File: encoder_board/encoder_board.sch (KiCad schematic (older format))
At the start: 4 parts, among them J1 Conn_01x06, U1 AS5048A

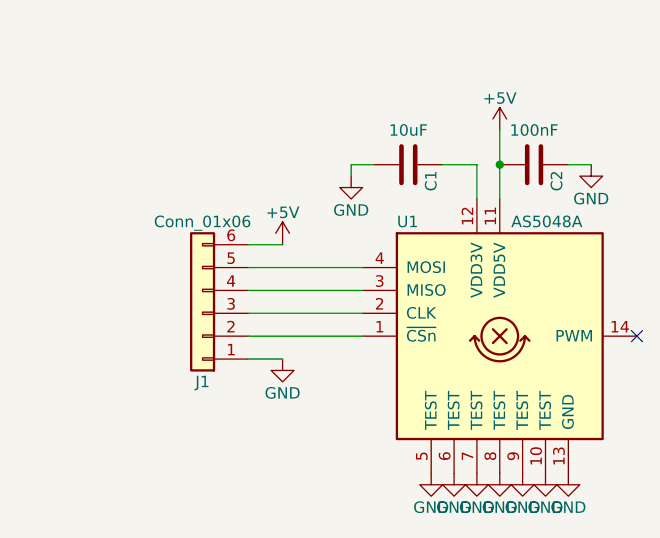
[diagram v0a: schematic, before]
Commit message: add footprint for small ir sensors
 - use 0402 in encoder board
 - still need to switch sensor board
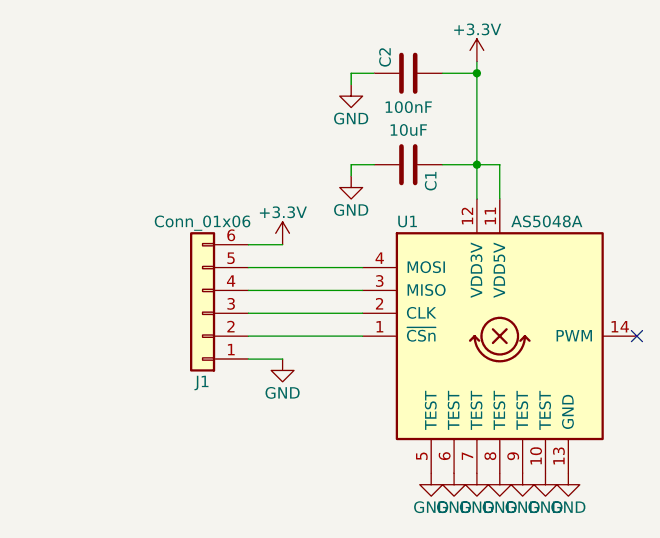
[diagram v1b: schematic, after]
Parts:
- C1, C2: footprint Capacitors_SMD:C_0603 -> Capacitors_SMD:C_0402
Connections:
- net +5V is gone; now on net +3V3: C2.2, J1.6 (Pin_6), U1.11 (VDD5V)
- net +3V3: now reaches C1.1, U1.12 (VDD3V)
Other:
- moved on the sheet: C2
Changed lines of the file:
@@
 LIBS:valves
 LIBS:motor_drivers
-LIBS:LED
 LIBS:sensors
+LIBS:encoder_board-cache
 EELAYER 25 0
 EELAYER END
@@
 F 0 "C1" H 5425 3200 50  0000 L CNN
 F 1 "10uF" V 5250 3100 50  0000 C CNN
-F 2 "Capacitors_SMD:C_0603" H 5438 2950 50  0001 C CNN
+F 2 "Capacitors_SMD:C_0402" H 5438 2950 50  0001 C CNN
 F 3 "" H 5400 3100 50  0001 C CNN
 	1    5400 3100
@@
 F 3 "" H 5150 3150 50  0001 C CNN
 	1    5150 3150
-	1    0    0    -1
-$EndComp
-$Comp
-L +5V #PWR09
-U 1 1 5AAA0D34
-P 5800 2950
-F 0 "#PWR09" H 5800 2800 50  0001 C CNN
-F 1 "+5V" H 5800 3090 50  0000 C CNN
-F 2 "" H 5800 2950 50  0001 C CNN
-F 3 "" H 5800 2950 50  0001 C CNN
-	1    5800 2950
 	1    0    0    -1
 $EndComp
@@
 $EndComp
 $Comp
-L +5V #PWR010
-U 1 1 5AAA0F91
-P 4850 3450
-F 0 "#PWR010" H 4850 3300 50  0001 C CNN
-F 1 "+5V" H 4850 3590 50  0000 C CNN
-F 2 "" H 4850 3450 50  0001 C CNN
-F 3 "" H 4850 3450 50  0001 C CNN
-	1    4850 3450
-	1    0    0    -1
-$EndComp
-$Comp
-L GND #PWR011
+L GND #PWR09
 U 1 1 5AAA0FBB
 P 4850 3950
-F 0 "#PWR011" H 4850 3700 50  0001 C CNN
+F 0 "#PWR09" H 4850 3700 50  0001 C CNN
 F 1 "GND" H 4850 3800 50  0000 C CNN
 F 2 "" H 4850 3950 50  0001 C CNN
@@
 L C C2
 U 1 1 5AAA1099
-P 5950 3100
-F 0 "C2" H 5975 3200 50  0000 L CNN
-F 1 "100nF" V 5800 3100 50  0000 C CNN
-F 2 "Capacitors_SMD:C_0603" H 5988 2950 50  0001 C CNN
-F 3 "" H 5950 3100 50  0001 C CNN
-	1    5950 3100
-	0    1    1    0
+P 5400 2700
+F 0 "C2" H 5425 2800 50  0000 L CNN
+F 1 "100nF" V 5250 2700 50  0000 C CNN
+F 2 "Capacitors_SMD:C_0402" H 5438 2550 50  0001 C CNN
+F 3 "" H 5400 2700 50  0001 C CNN
+	1    5400 2700
+	0    -1   -1   0
 $EndComp
 NoConn ~ 6400 3850
 $Comp
-L GND #PWR012
+L GND #PWR010
 U 1 1 5AAA1198
-P 6200 3100
-F 0 "#PWR012" H 6200 2850 50  0001 C CNN
-F 1 "GND" H 6200 2950 50  0000 C CNN
-F 2 "" H 6200 3100 50  0001 C CNN
-F 3 "" H 6200 3100 50  0001 C CNN
-	1    6200 3100
-	1    0    0    -1
-$EndComp
-Wire Wire Line
-	5550 3100 5700 3100
-Wire Wire Line
-	5700 3100 5700 3250
+P 5150 2750
+F 0 "#PWR010" H 5150 2500 50  0001 C CNN
+F 1 "GND" H 5150 2600 50  0000 C CNN
+F 2 "" H 5150 2750 50  0001 C CNN
+F 3 "" H 5150 2750 50  0001 C CNN
+	1    5150 2750
+	1    0    0    -1
+$EndComp
+$Comp
+L +3.3V #PWR011
+U 1 1 5AAC3FB7
+P 5700 2650
+F 0 "#PWR011" H 5700 2500 50  0001 C CNN
+F 1 "+3.3V" H 5700 2790 50  0000 C CNN
+F 2 "" H 5700 2650 50  0001 C CNN
+F 3 "" H 5700 2650 50  0001 C CNN
+	1    5700 2650
+	1    0    0    -1
+$EndComp
+$Comp
+L +3.3V #PWR012
+U 1 1 5AAC405B
+P 4850 3450
+F 0 "#PWR012" H 4850 3300 50  0001 C CNN
+F 1 "+3.3V" H 4850 3590 50  0000 C CNN
+F 2 "" H 4850 3450 50  0001 C CNN
+F 3 "" H 4850 3450 50  0001 C CNN
+	1    4850 3450
+	1    0    0    -1
+$EndComp
 Wire Wire Line
 	5150 3150 5150 3100
@@
 	5200 3850 4700 3850
 Wire Wire Line
-	5800 2950 5800 3250
-Connection ~ 5800 3100
-Wire Wire Line
-	6100 3100 6200 3100
+	5550 2700 5700 2700
+Wire Wire Line
+	5250 2700 5150 2700
+Wire Wire Line
+	5150 2700 5150 2750
+Wire Wire Line
+	5700 2650 5700 3250
+Connection ~ 5700 2700
+Wire Wire Line
+	5550 3100 5800 3100
+Connection ~ 5700 3100
+Wire Wire Line
+	5800 3100 5800 3250
 $EndSCHEMATC

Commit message: use named nets
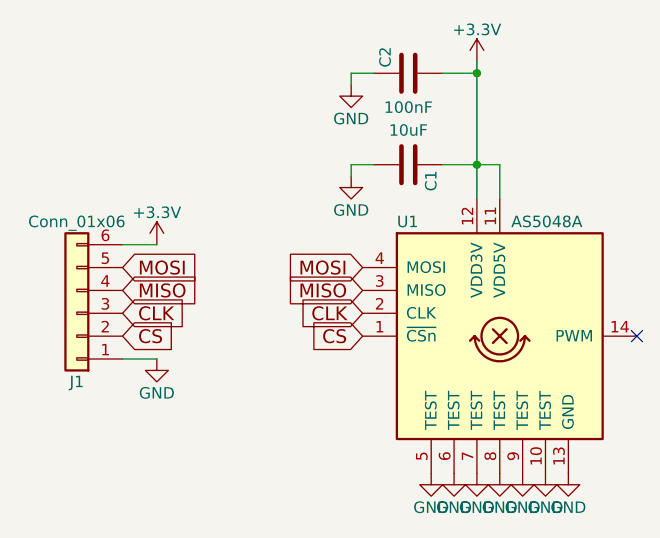
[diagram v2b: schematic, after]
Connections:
- net CS: now reaches J1.2 (Pin_2), U1.1 (~CSn)
- net CLK: now reaches J1.3 (Pin_3), U1.2 (CLK)
- net MISO: now reaches J1.4 (Pin_4), U1.3 (MISO)
- net MOSI: now reaches J1.5 (Pin_5), U1.4 (MOSI)
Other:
- moved on the sheet: J1
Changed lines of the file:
@@
 LIBS:valves
 LIBS:motor_drivers
+LIBS:LED
 LIBS:sensors
 LIBS:encoder_board-cache
@@
 L Conn_01x06 J1
 U 1 1 5AAA0E35
-P 4500 3750
-F 0 "J1" H 4500 4050 50  0000 C CNN
-F 1 "Conn_01x06" H 4500 3350 50  0000 C CNN
-F 2 "Pin_Headers:Pin_Header_Straight_1x06_Pitch1.27mm" H 4500 3750 50  0001 C CNN
-F 3 "" H 4500 3750 50  0001 C CNN
-	1    4500 3750
+P 3950 3750
+F 0 "J1" H 3950 4050 50  0000 C CNN
+F 1 "Conn_01x06" H 3950 3350 50  0000 C CNN
+F 2 "Pin_Headers:Pin_Header_Straight_1x06_Pitch1.27mm" H 3950 3750 50  0001 C CNN
+F 3 "" H 3950 3750 50  0001 C CNN
+	1    3950 3750
 	-1   0    0    1
 $EndComp
@@
 L GND #PWR09
 U 1 1 5AAA0FBB
-P 4850 3950
-F 0 "#PWR09" H 4850 3700 50  0001 C CNN
-F 1 "GND" H 4850 3800 50  0000 C CNN
-F 2 "" H 4850 3950 50  0001 C CNN
-F 3 "" H 4850 3950 50  0001 C CNN
-	1    4850 3950
+P 4300 3950
+F 0 "#PWR09" H 4300 3700 50  0001 C CNN
+F 1 "GND" H 4300 3800 50  0000 C CNN
+F 2 "" H 4300 3950 50  0001 C CNN
+F 3 "" H 4300 3950 50  0001 C CNN
+	1    4300 3950
 	1    0    0    -1
 $EndComp
@@
 L +3.3V #PWR012
 U 1 1 5AAC405B
-P 4850 3450
-F 0 "#PWR012" H 4850 3300 50  0001 C CNN
-F 1 "+3.3V" H 4850 3590 50  0000 C CNN
-F 2 "" H 4850 3450 50  0001 C CNN
-F 3 "" H 4850 3450 50  0001 C CNN
-	1    4850 3450
+P 4300 3450
+F 0 "#PWR012" H 4300 3300 50  0001 C CNN
+F 1 "+3.3V" H 4300 3590 50  0000 C CNN
+F 2 "" H 4300 3450 50  0001 C CNN
+F 3 "" H 4300 3450 50  0001 C CNN
+	1    4300 3450
 	1    0    0    -1
 $EndComp
@@
 	5150 3100 5250 3100
 Wire Wire Line
-	4850 3450 4700 3450
-Wire Wire Line
-	4850 3950 4700 3950
-Wire Wire Line
-	5200 3550 4700 3550
-Wire Wire Line
-	5200 3650 4700 3650
-Wire Wire Line
-	4700 3750 5200 3750
-Wire Wire Line
-	5200 3850 4700 3850
+	4300 3450 4150 3450
+Wire Wire Line
+	4300 3950 4150 3950
 Wire Wire Line
 	5550 2700 5700 2700
@@
 Wire Wire Line
 	5800 3100 5800 3250
+Text GLabel 5200 3550 0    60   Input ~ 0
+MOSI
+Text GLabel 5200 3650 0    60   Input ~ 0
+MISO
+Text GLabel 5200 3750 0    60   Input ~ 0
+CLK
+Text GLabel 5200 3850 0    60   Input ~ 0
+CS
+Text GLabel 4150 3850 2    60   Input ~ 0
+CS
+Text GLabel 4150 3750 2    60   Input ~ 0
+CLK
+Text GLabel 4150 3650 2    60   Input ~ 0
+MISO
+Text GLabel 4150 3550 2    60   Input ~ 0
+MOSI
 $EndSCHEMATC

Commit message: reviewer final encoder board.
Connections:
- net +3V3: now also J1.2 (Pin_2); no longer J1.6 (Pin_6)
- net CLK: now also J1.4 (Pin_4); no longer J1.3 (Pin_3)
- net CS: now also J1.3 (Pin_3); no longer J1.2 (Pin_2)
- net GND: no longer U1.10 (TEST), U1.6 (TEST), U1.7 (TEST), U1.8 (TEST), U1.9 (TEST)
- net MISO: now also J1.5 (Pin_5); no longer J1.4 (Pin_4)
- net MOSI: now also J1.6 (Pin_6); no longer J1.5 (Pin_5)
- no-connect marks 1 -> 6
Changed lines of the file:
@@
-$EndComp
-$Comp
-L GND #PWR01
-U 1 1 5AAA0BB0
-P 6000 4450
-F 0 "#PWR01" H 6000 4200 50  0001 C CNN
-F 1 "GND" H 6000 4300 50  0000 C CNN
-F 2 "" H 6000 4450 50  0001 C CNN
-F 3 "" H 6000 4450 50  0001 C CNN
-	1    6000 4450
-	1    0    0    -1
-$EndComp
-$Comp
-L GND #PWR02
-U 1 1 5AAA0BC6
-P 5900 4450
-F 0 "#PWR02" H 5900 4200 50  0001 C CNN
-F 1 "GND" H 5900 4300 50  0000 C CNN
-F 2 "" H 5900 4450 50  0001 C CNN
-F 3 "" H 5900 4450 50  0001 C CNN
-	1    5900 4450
-	1    0    0    -1
-$EndComp
-$Comp
-L GND #PWR03
-U 1 1 5AAA0BDC
-P 5800 4450
-F 0 "#PWR03" H 5800 4200 50  0001 C CNN
-F 1 "GND" H 5800 4300 50  0000 C CNN
-F 2 "" H 5800 4450 50  0001 C CNN
-F 3 "" H 5800 4450 50  0001 C CNN
-	1    5800 4450
-	1    0    0    -1
-$EndComp
-$Comp
-L GND #PWR04
-U 1 1 5AAA0BF2
-P 5700 4450
-F 0 "#PWR04" H 5700 4200 50  0001 C CNN
-F 1 "GND" H 5700 4300 50  0000 C CNN
-F 2 "" H 5700 4450 50  0001 C CNN
-F 3 "" H 5700 4450 50  0001 C CNN
-	1    5700 4450
-	1    0    0    -1
-$EndComp
-$Comp
-L GND #PWR05
-U 1 1 5AAA0C08
-P 5600 4450
-F 0 "#PWR05" H 5600 4200 50  0001 C CNN
-F 1 "GND" H 5600 4300 50  0000 C CNN
-F 2 "" H 5600 4450 50  0001 C CNN
-F 3 "" H 5600 4450 50  0001 C CNN
-	1    5600 4450
-	1    0    0    -1
-$EndComp
-$Comp
-L GND #PWR06
-U 1 1 5AAA0C1E
-P 5500 4450
-F 0 "#PWR06" H 5500 4200 50  0001 C CNN
-F 1 "GND" H 5500 4300 50  0000 C CNN
-F 2 "" H 5500 4450 50  0001 C CNN
-F 3 "" H 5500 4450 50  0001 C CNN
-	1    5500 4450
-	1    0    0    -1
 $EndComp
 $Comp
@@
 L +3.3V #PWR012
 U 1 1 5AAC405B
-P 4300 3450
-F 0 "#PWR012" H 4300 3300 50  0001 C CNN
-F 1 "+3.3V" H 4300 3590 50  0000 C CNN
-F 2 "" H 4300 3450 50  0001 C CNN
-F 3 "" H 4300 3450 50  0001 C CNN
-	1    4300 3450
+P 4550 3850
+F 0 "#PWR012" H 4550 3700 50  0001 C CNN
+F 1 "+3.3V" H 4550 3990 50  0000 C CNN
+F 2 "" H 4550 3850 50  0001 C CNN
+F 3 "" H 4550 3850 50  0001 C CNN
+	1    4550 3850
 	1    0    0    -1
 $EndComp
@@
 Wire Wire Line
 	5150 3100 5250 3100
-Wire Wire Line
-	4300 3450 4150 3450
 Wire Wire Line
 	4300 3950 4150 3950
@@
 Text GLabel 5200 3850 0    60   Input ~ 0
 CS
-Text GLabel 4150 3850 2    60   Input ~ 0
+Text GLabel 4150 3750 2    60   Input ~ 0
 CS
-Text GLabel 4150 3750 2    60   Input ~ 0
+Text GLabel 4150 3650 2    60   Input ~ 0
 CLK
-Text GLabel 4150 3650 2    60   Input ~ 0
+Text GLabel 4150 3550 2    60   Input ~ 0
 MISO
-Text GLabel 4150 3550 2    60   Input ~ 0
+Text GLabel 4150 3450 2    60   Input ~ 0
 MOSI
+$Comp
+L GND #PWR06
+U 1 1 5AAA0C1E
+P 5500 4450
+F 0 "#PWR06" H 5500 4200 50  0001 C CNN
+F 1 "GND" H 5500 4300 50  0000 C CNN
+F 2 "" H 5500 4450 50  0001 C CNN
+F 3 "" H 5500 4450 50  0001 C CNN
+	1    5500 4450
+	1    0    0    -1
+$EndComp
+NoConn ~ 6000 4450
+NoConn ~ 5900 4450
+NoConn ~ 5800 4450
+NoConn ~ 5700 4450
+NoConn ~ 5600 4450
+Wire Wire Line
+	4150 3850 4550 3850
 $EndSCHEMATC
